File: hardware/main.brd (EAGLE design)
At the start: 87.6 x 68.1 mm, 60 parts, among them CON1 WIRE2BOARD_10POS, CON2 WIRE2BOARD_10POS, U1 SN74LVC4245A_DW_24, U2 Value, U3 SN74ABT541B_DW_20, U4 SN74LVC1G04_DBV_5, U5 SN74LVC4245A_DW_24, U6 Value, U7 TXB0101_DBV_6, U8 8BIT-DIP-SWITCH, U9 LM3940SOT223

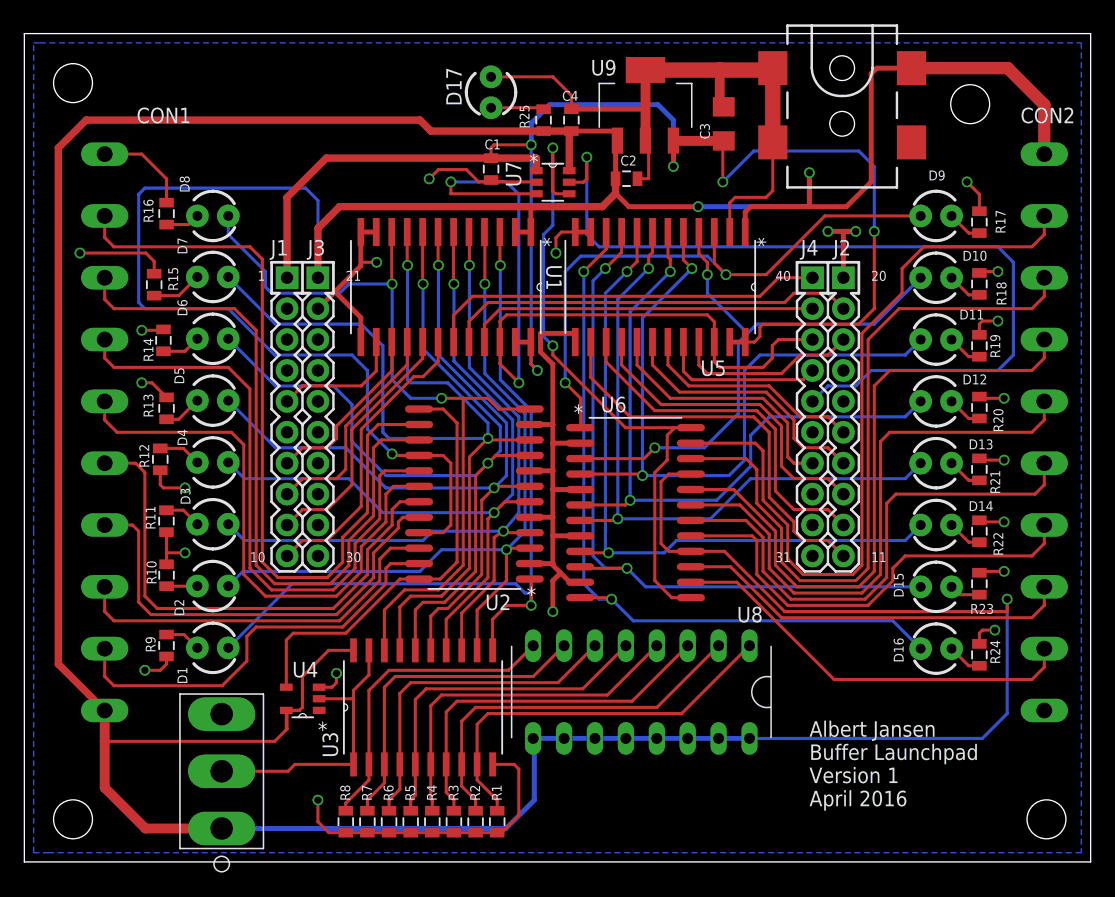
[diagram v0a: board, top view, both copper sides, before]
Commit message: Added pulldown resistors on inputs. Updated version number
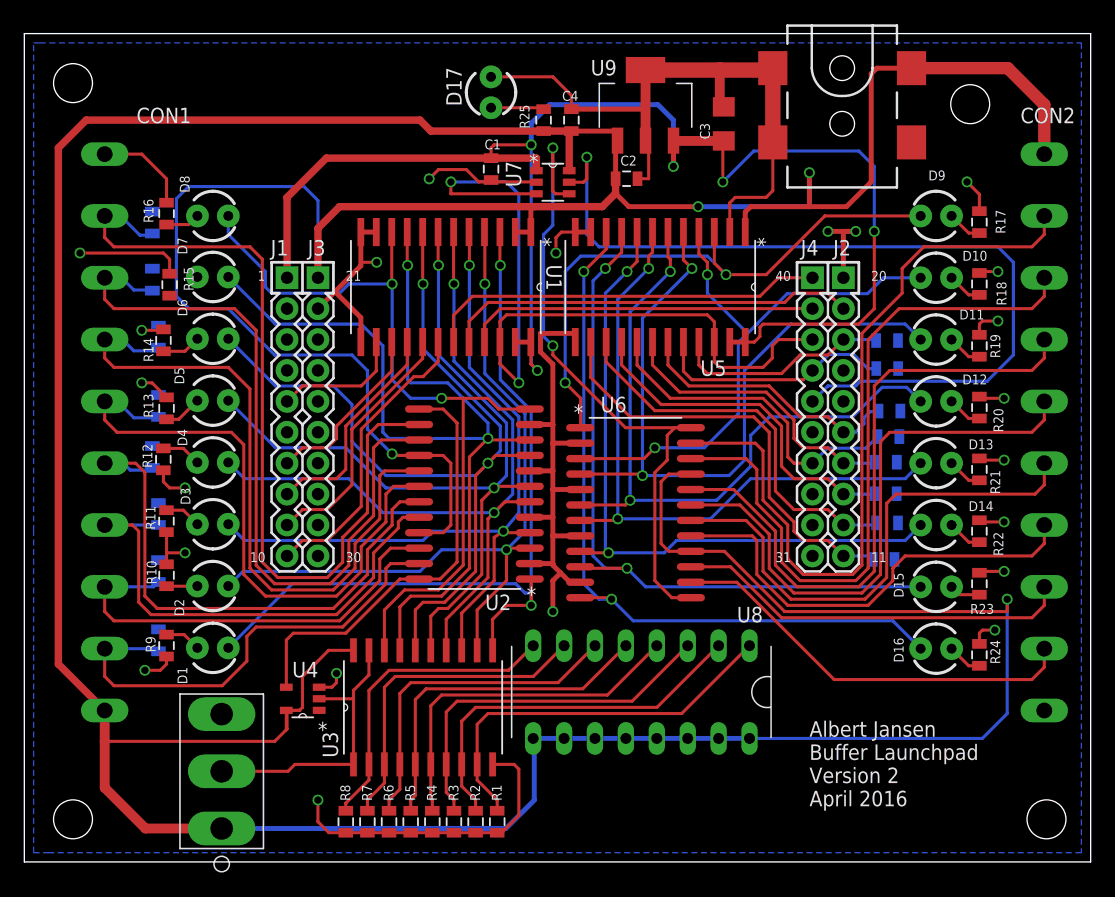
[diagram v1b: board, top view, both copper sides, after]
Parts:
- added R26, R27, R28, R29, R30, R31, R32, R33, R34, R35, R36, R37, R38, R39, R40, R41: 10k, SparkFun-Resistors:0805
- moved R15 1.27 mm to (11.9, 47.4)
- moved R12 0.25 mm to (11.4, 33.1)
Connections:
- net GND: now also R26.1, R27.1, R28.1, R29.1, R30.1, R31.1, R32.1, R33.1, R34.1, R35.1, R36.1, R37.1, R38.1, R39.1, R40.1, R41.1
- net N$1: now also R29.2
- net N$2: now also R28.2
- net N$3: now also R27.2
- net N$4: now also R26.2
- net N$5: now also R30.2
- net N$6: now also R31.2
- net N$7: now also R32.2
- net N$8: now also R33.2
- net UCOUT1: now also R41.2
- net UCOUT2: now also R40.2
- net UCOUT3: now also R39.2
- net UCOUT4: now also R38.2
- net UCOUT5: now also R37.2
- net UCOUT6: now also R36.2
- net UCOUT7: now also R35.2
- net UCOUT8: now also R34.2
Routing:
- net 5V: track 439.6 -> 433.0 mm
- net UCOUT2: track 13.6 -> 19.9 mm
- net UCOUT5: track 21.3 -> 27.5 mm
- net N$1: track 45.9 -> 50.9 mm
- net N$2: track 51.2 -> 56.1 mm
- net N$4: track 63.9 -> 68.5 mm
- net N$7: track 31.7 -> 36.3 mm
- net N$8: track 34.6 -> 39.1 mm
- net N$6: track 37.1 -> 41.5 mm
- net N$3: track 58.0 -> 62.3 mm
- net N$5: track 42.3 -> 46.5 mm
- net N$15: track 4.18 -> 0.00 mm
- net UCOUT3: track 18.6 -> 22.5 mm
- net UCOUT7: track 29.7 -> 32.4 mm
- net UCOUT1: track 15.2 -> 17.9 mm
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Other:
- board text added: "Albert Jansen Buffer Launchpad Version 2 April 2016"
- board text removed: "Albert Jansen Buffer Launchpad Version 1 April 2016"

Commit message: Re-routed and updated board and schematic
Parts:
- removed C1, C2: 0.1uF, SparkFun-Capacitors:0805
- removed CON1, CON2: WIRE2BOARD_10POS, ControllerCard:WIRE2BOARD_SCREW
- removed R1, R2, R26, R27, R28, R29, R3, R30, R31, R32, R33, R34, R35, R36, R37, R38, R39, R4, R40, R41, R5, R6, R7, R8: 10k, SparkFun-Resistors:0805
- removed U2, U6: Value, ControllerCard:DW0024A_N
- removed U3: SN74ABT541B_DW_20, ControllerCard:DW20
- removed U4: SN74LVC1G04_DBV_5, ControllerCard:DBV5
- removed U7: TXB0101_DBV_6, ControllerCard:DBV6
- removed U8: 8BIT-DIP-SWITCH, ControllerCard:SPST-DIPS-SW
- added U$1, U$3, U$4: 4PIN_SOCKET, ControllerCard:CONN-4PIN
- added U$5, U$6: 2PIN_SOCKET, ControllerCard:CONN-2PIN
- added U$7, U$8: RESISTOR_ARRAY, ControllerCard:DIL16
- R10, R11, R12, R13, R14, R15, R16, R9: value 300 -> 330
- R25: value 300 -> 4.7k
- U$2: value M2-SWITCH -> 4PIN_SOCKET; device ControllerCard:M2-TOGGLE-SW -> ControllerCard:CONN-4PIN
- moved U$2 67.1 mm to (83.1, 12.6), turned to 270 degrees
- moved R16 49.0 mm to (11.9, 4.25)
- moved D8 48.0 mm to (15.7, 5.08)
- moved R15 38.1 mm to (11.9, 9.33)
- moved D7 37.8 mm to (15.7, 10.2)
- moved R14 28.5 mm to (11.9, 14.4)
- moved D6 27.7 mm to (15.7, 15.3)
- moved D1 23.1 mm to (15.7, 40.7)
- moved R9 22.1 mm to (11.9, 39.9), turned to 90 degrees
- moved R13 17.8 mm to (11.9, 19.5)
- moved D5 17.5 mm to (15.7, 20.4)
- moved R23 13.5 mm to (77.5, 9.41)
- moved D2 13.0 mm to (15.7, 35.6)
- moved R17 12.7 mm to (77.5, 39.9)
- moved R20 12.7 mm to (77.5, 24.7)
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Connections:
- removed net !INSEL!: U2.13, U2.24, U4.4
- removed net !OUTBUFEN!: U6.13, U6.24, U7.4
- removed net INSEL: U$2.2, U3.1, U3.19, U4.2
- removed net LEDIN1: D1.A, U1.3, U2.1, U3.11
- removed net LEDIN2: D2.A, U1.4, U2.3, U3.12
- removed net LEDIN3: D3.A, U1.5, U2.4, U3.13
- removed net LEDIN4: D4.A, U1.6, U2.6, U3.14
- removed net LEDIN5: D5.A, U1.7, U2.7, U3.15
- removed net LEDIN6: D6.A, U1.8, U2.9, U3.16
- removed net LEDIN7: D7.A, U1.9, U2.10, U3.17
- removed net LEDIN8: D8.A, U1.10, U2.12, U3.18
- removed net LEDOUT1: D9.A, U5.3, U6.1
- removed net LEDOUT2: D10.A, U5.4, U6.3
- removed net LEDOUT3: D11.A, U5.5, U6.4
- removed net LEDOUT4: D12.A, U5.6, U6.6
- removed net LEDOUT5: D13.A, U5.7, U6.7
- removed net LEDOUT6: D14.A, U5.8, U6.9
- removed net LEDOUT7: D15.A, U5.9, U6.10
- removed net LEDOUT8: D16.A, U5.10, U6.12
- removed net SW1: R1.2, U3.9, U8.1
- removed net SW2: R2.2, U3.8, U8.2
- removed net SW3: R3.2, U3.7, U8.3
- removed net SW4: R4.2, U3.6, U8.4
- removed net SW5: R5.2, U3.5, U8.5
- removed net SW6: R6.2, U3.4, U8.6
- removed net SW7: R7.2, U3.3, U8.7
- removed net SW8: R8.2, U3.2, U8.8
- net !BUFEN!: now also A1.18; no longer A1.38, U7.3
- net 3.3V: now also R25.1; no longer C1.1, U7.1
- net 5V: now also U$5.P$1, U$6.P$1; no longer A1.21, C2.1, CON1.10, CON2.10, R25.1, U$2.1, U2.16, U2.21, U3.20, U4.5, U6.16, U6.21, U7.6, U8.10, U8.11, U8.12, U8.13, U8.14, U8.15, U8.16, U8.9
- net ENEXT: no longer U7.5
- net GND: now also U$5.P$2, U$6.P$2, U$7.10, U$7.11, U$7.12, U$7.13, U$7.14, U$7.15, U$7.16, U$7.9, U$8.10, U$8.11, U$8.12, U$8.13, U$8.14, U$8.15, U$8.16, U$8.9; no longer C1.2, C2.2, CON1.1, CON2.1, R1.1, R2.1, R26.1, R27.1, R28.1, R29.1, R3.1, R30.1, R31.1, R32.1, R33.1, R34.1, R35.1, R36.1, R37.1, R38.1, R39.1, R4.1, R40.1, R41.1, R5.1, R6.1, R7.1, R8.1, U$2.3, U2.11, U2.2, U2.5, U2.8, U3.10, U4.3, U6.11, U6.2, U6.5, U6.8, U7.2
- net N$1: now also U$1.P1, U$7.1, U1.10; no longer CON1.5, R29.2, U2.18
- net N$17: now also U$4.P1, U5.3; no longer CON2.5, U6.18
- net N$18: now also U$4.P2, U5.4; no longer CON2.4, U6.17
- net N$19: now also U$4.P3, U5.5; no longer CON2.3, U6.15
- net N$2: now also U$1.P2, U$7.2, U1.9; no longer CON1.4, R28.2, U2.17
- net N$20: now also U$4.P4, U5.6; no longer CON2.2, U6.14
- net N$21: now also U$2.P1, U5.7; no longer CON2.6, U6.19
- net N$22: now also U$2.P2, U5.8; no longer CON2.7, U6.20
- net N$23: now also U$2.P3, U5.9; no longer CON2.8, U6.22
- net N$24: now also U$2.P4, U5.10; no longer CON2.9, U6.23
- net N$3: now also U$1.P3, U$7.3, U1.8; no longer CON1.3, R27.2, U2.15
- net N$4: now also U$1.P4, U$7.4, U1.7; no longer CON1.2, R26.2, U2.14
- net N$5: now also U$3.P1, U$7.5, U1.6; no longer CON1.6, R30.2, U2.19
- net N$6: now also U$3.P2, U$7.6, U1.5; no longer CON1.7, R31.2, U2.20
- net N$7: now also U$3.P3, U$7.7, U1.4; no longer CON1.8, R32.2, U2.22
- net N$8: now also U$3.P4, U$7.8, U1.3; no longer CON1.9, R33.2, U2.23
- net UCIN1: now also A1.19, D1.A; no longer A1.39
- net UCIN2: now also A1.40, D2.A; no longer A1.19
- net UCIN3: now also A1.39, D3.A; no longer A1.40
- net UCIN4: now also A1.5, D4.A; no longer A1.10
- net UCIN5: now also A1.7, D5.A; no longer A1.9
- net UCIN6: now also D6.A
- net UCIN7: now also A1.9, D7.A; no longer A1.7
- net UCIN8: now also A1.10, D8.A; no longer A1.5
- net UCOUT1: now also A1.38, D9.A, U$8.1; no longer A1.18, R41.2
- net UCOUT2: now also D10.A, U$8.2; no longer R40.2
- net UCOUT3: now also D11.A, U$8.3; no longer R39.2
- net UCOUT4: now also D12.A, U$8.4; no longer R38.2
- net UCOUT5: now also D13.A, U$8.5; no longer R37.2
- net UCOUT6: now also D14.A, U$8.6; no longer R36.2
- net UCOUT7: now also D15.A, U$8.7; no longer R35.2
- net UCOUT8: now also D16.A, U$8.8; no longer R34.2
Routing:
- net 5V: track 433.0 -> 122.4 mm
- net LEDIN7: track 78.0 -> 0.00 mm, vias 2 -> 0
- net LEDIN6: track 72.9 -> 0.00 mm, vias 2 -> 0
- net ENEXT: track 71.4 -> 0.00 mm, vias 1 -> 0
- net LEDIN8: track 67.6 -> 0.00 mm, vias 2 -> 0
- net LEDIN1: track 67.6 -> 0.00 mm, vias 2 -> 0
- net LEDIN5: track 67.5 -> 0.00 mm, vias 2 -> 0
- net LEDIN4: track 65.5 -> 0.00 mm, vias 2 -> 0
- net LEDIN3: track 64.0 -> 0.00 mm, vias 2 -> 0
- net LEDIN2: track 63.5 -> 0.00 mm, vias 2 -> 0
- net LEDOUT8: track 62.3 -> 0.00 mm, vias 2 -> 0
- net 3.3V: track 123.7 -> 61.8 mm
- net LEDOUT3: track 60.0 -> 0.00 mm, vias 2 -> 0
- net LEDOUT7: track 59.5 -> 0.00 mm, vias 2 -> 0
- net LEDOUT4: track 57.4 -> 0.00 mm, vias 2 -> 0
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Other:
- board size 87.6 x 68.1 mm -> 87.6 x 56.6 mm
